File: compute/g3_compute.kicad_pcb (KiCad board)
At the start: 4 copper layers, 100 x 100 mm, 36 parts, among them J101 CONSMA001-SMD-G, U101 PA1616D, U102 LoRa-E5, U201 SX1262, U202 PE4259, Y201 DNL

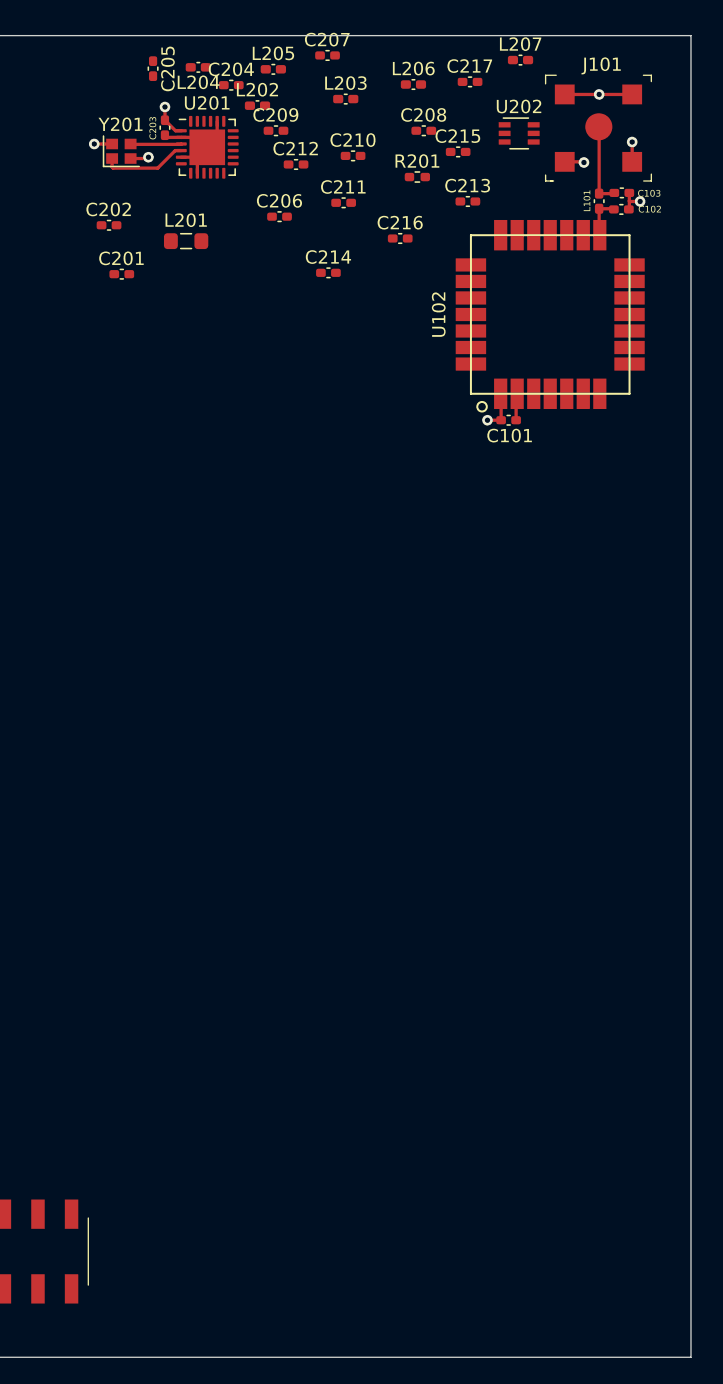
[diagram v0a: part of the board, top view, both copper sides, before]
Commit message: Finish LoRa routing
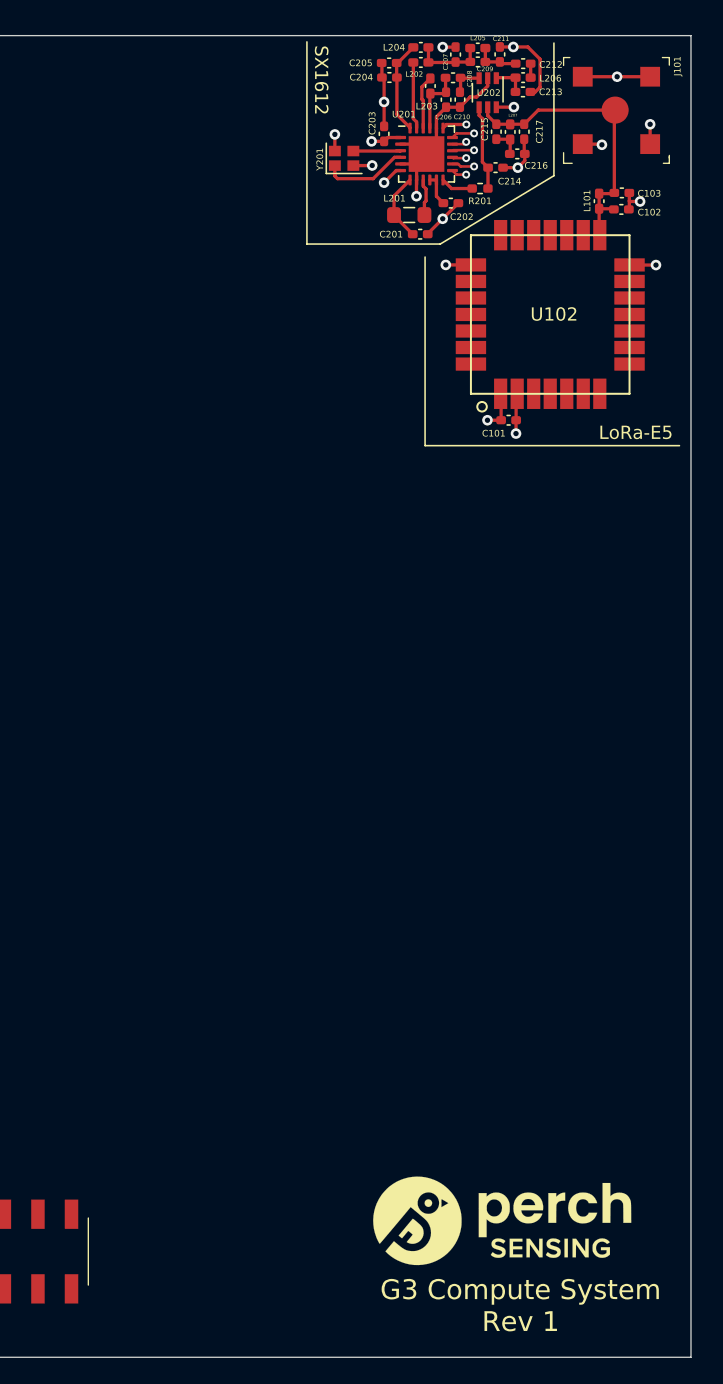
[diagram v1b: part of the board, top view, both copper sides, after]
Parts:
- added G***: LOGO, Perch:perch_logo, F.Cu at (185.8, 129.8)
- moved C202 25.9 mm to (181.8, 52.7)
- moved C201 22.8 mm to (179.5, 55.0)
- moved C212 18.8 mm to (187.3, 42.1)
- moved C205 17.9 mm to (177.2, 42.1), turned to 180 degrees
- moved L201 17.0 mm to (178.7, 53.6)
- moved L204 16.9 mm to (179.6, 40.9)
- moved Y201 16.9 mm to (173.8, 49.3)
- moved U201 16.6 mm to (180.0, 49.0)
- moved C203 16.6 mm to (176.8, 47.4), turned to 90 degrees
- moved C211 16.3 mm to (185.5, 41.4), turned to 90 degrees
- moved C209 16.1 mm to (183.9, 42.0)
- moved L205 15.6 mm to (183.9, 40.9)
- moved C206 15.4 mm to (181.5, 44.9), turned to 270 degrees
- moved C214 14.9 mm to (185.2, 50.0)
- moved L202 12.8 mm to (179.6, 42.0)
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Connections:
- C215 pad 1: Net-(C215-Pad1) -> /ANT
- U202 pad 5: Net-(C215-Pad1) -> /ANT
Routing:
- net GND: track 24.3 -> 54.5 mm, vias 6 -> 15
- net /ANT: track 9.39 -> 22.9 mm
- net Net-(C204-Pad1): track 0.00 -> 7.09 mm
- net Net-(C214-Pad1): track 0.00 -> 6.44 mm
- net Net-(C207-Pad1): track 0.00 -> 5.38 mm
- net Net-(C201-Pad1): track 0.00 -> 5.19 mm
- net Net-(L202-Pad1): track 0.00 -> 5.07 mm
- net Net-(C206-Pad1): track 0.00 -> 4.97 mm
- net Net-(L203-Pad1): track 0.00 -> 4.14 mm
- net Net-(C209-Pad2): track 0.00 -> 3.58 mm
- net Net-(L201-Pad2): track 0.00 -> 2.79 mm
- net Net-(C213-Pad1): track 0.00 -> 2.60 mm
- net Net-(C208-Pad2): track 0.00 -> 2.52 mm
- net /LoRa Module/DIO2: track 0.00 -> 2.47 mm
- net Net-(C202-Pad1): track 0.00 -> 2.47 mm
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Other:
- board text added: "G3 Compute System Rev 1"
- board text added: "LoRa-E5"
- board text added: "SX1612"

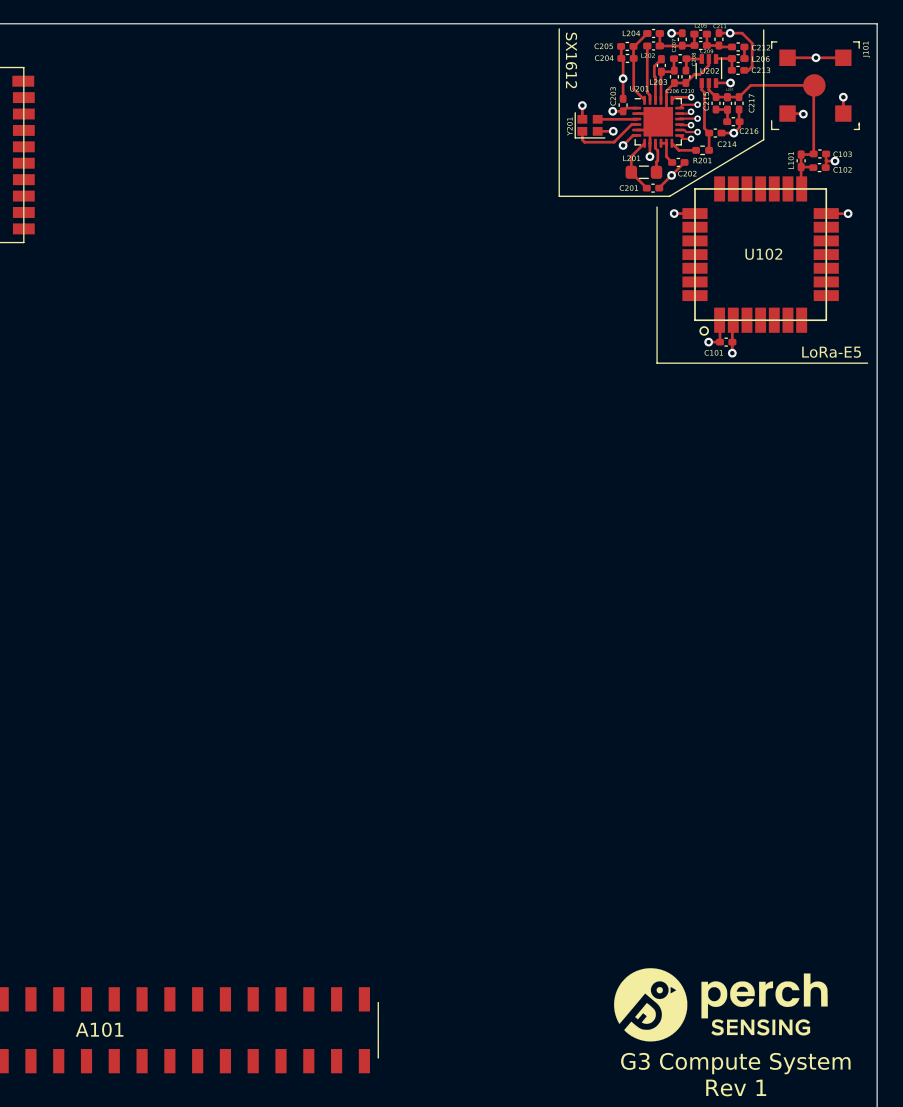
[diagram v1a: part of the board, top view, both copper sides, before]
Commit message: Fixing libraries and schematic ref nums
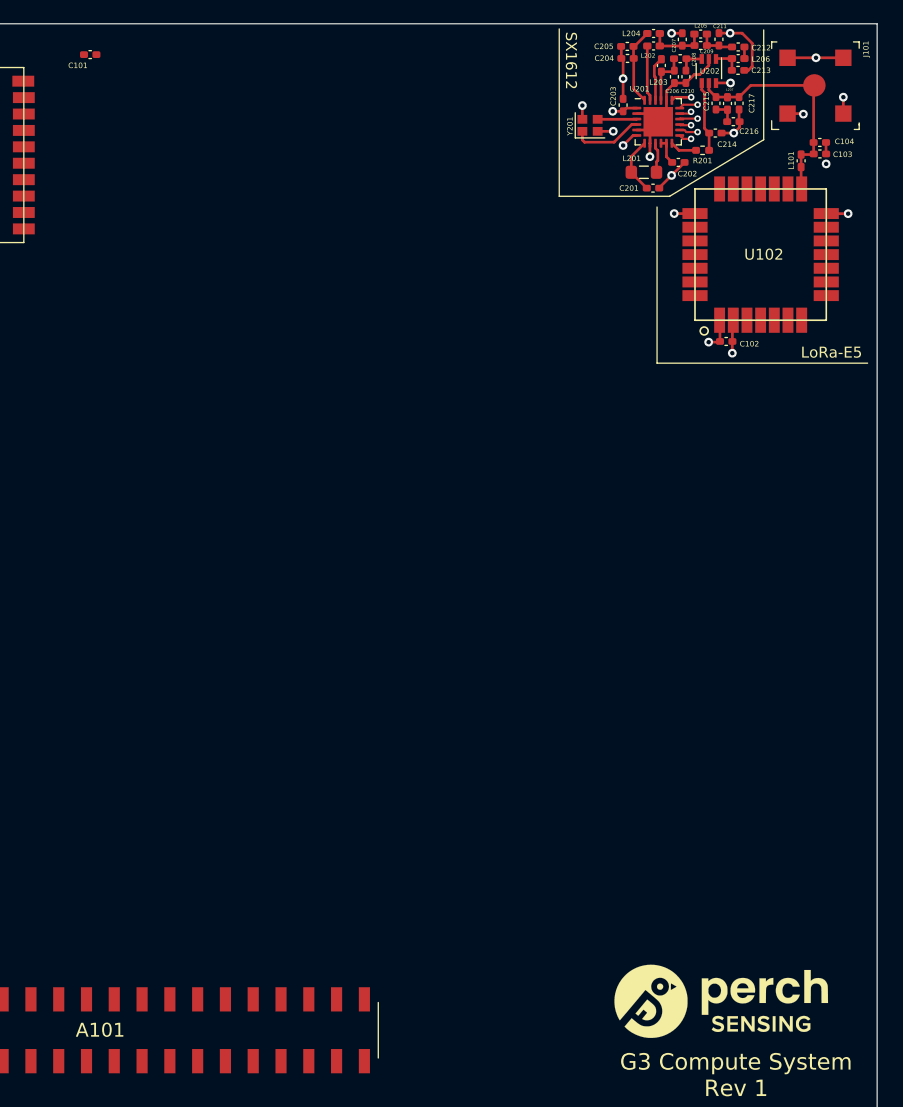
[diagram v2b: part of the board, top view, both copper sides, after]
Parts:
- added C104: DNL, Capacitor_SMD:C_0402_1005Metric_Pad0.74x0.62mm_HandSolder, F.Cu at (194.8, 50.9)
- C102: value DNL -> 4.7uF
- moved C101 63.8 mm to (128.1, 42.8)
- moved C102 18.0 mm to (186.2, 69.0)
- moved G*** 0.32 mm to (185.9, 129.4)
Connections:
- net Net-(U101-Pad1) renamed /GPS_Switch/VOUT
- net Net-(U101-Pad2) renamed /~GPS_RESET
- C102 pad 1: /ANT -> 3V3
- U101 pad 12: Net-(U101-Pad12) -> GND
- U101 pad 19: Net-(U101-Pad19) -> GND
- U101 pad 8: Net-(U101-Pad8) -> Net-(U101-Pad3)
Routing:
- net GND: track 54.5 -> 53.4 mm
- net /ANT: track 22.9 -> 21.9 mm

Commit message: rework on sch and layout
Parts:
- added C101: 1uF, Capacitor_SMD:C_0402_1005Metric_Pad0.74x0.62mm_HandSolder, F.Cu at (128.7, 79.1)
- added C105: 1uF, Capacitor_SMD:C_0402_1005Metric_Pad0.74x0.62mm_HandSolder, F.Cu at (125.4, 83.0)
- added J102: Temp_Connector_1x4, Perch:1702474_Temp_Sensor_Connector, F.Cu at (112.1, 74.9)
- added R101: 470, Resistor_SMD:R_0402_1005Metric_Pad0.72x0.64mm_HandSolder, F.Cu at (125.4, 73.1)
- added R102: 470, Resistor_SMD:R_0402_1005Metric_Pad0.72x0.64mm_HandSolder, F.Cu at (125.4, 75.1)
- added R103: TBD, Resistor_SMD:R_0402_1005Metric_Pad0.72x0.64mm_HandSolder, F.Cu at (128.7, 73.1)
- added R104: TBD, Resistor_SMD:R_0402_1005Metric_Pad0.72x0.64mm_HandSolder, F.Cu at (125.4, 77.1)
- added R105: 0, Resistor_SMD:R_0402_1005Metric_Pad0.72x0.64mm_HandSolder, F.Cu at (128.7, 75.1)
- added R106: 0, Resistor_SMD:R_0402_1005Metric_Pad0.72x0.64mm_HandSolder, F.Cu at (125.4, 79.1)
- added R107: 22, Resistor_SMD:R_0402_1005Metric_Pad0.72x0.64mm_HandSolder, F.Cu at (128.7, 77.1)
- added R108: 22, Resistor_SMD:R_0402_1005Metric_Pad0.72x0.64mm_HandSolder, F.Cu at (125.4, 81.1)
- renumbered C101 to C102
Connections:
- net /LoRa Module/SCK renamed /PI_SCLK
- net /LoRa Module/SDI renamed /PI_SDO
- net /LoRa Module/~CS renamed /~PI_CE0
- net /LoRa Module/~RESET renamed /~SX_RESET
- net Net-(U102-Pad17) renamed /~E5_RESET
- C103 pad 1: /ANT -> /E5_RFIO
- L101 pad 1: /ANT -> /E5_RFIO
- U101 pad 1: /GPS_Switch/VOUT -> /GPS_VCC
- U101 pad 10: Net-(R102-Pad1) -> /GPS_RX0
- U101 pad 3: Net-(U101-Pad3) -> GND
- U101 pad 8: Net-(U101-Pad3) -> GND
- U101 pad 9: Net-(R101-Pad1) -> /GPS_TX0
- U102 pad 10: Net-(U102-Pad10) -> /E5_TX
- U102 pad 15: /ANT -> /E5_RFIO
- U102 pad 9: Net-(U102-Pad9) -> /E5_RX
- U201 pad 16: /LoRa Module/SDO -> /PI_SDI
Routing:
- net /PI_SDI: track 0.00 -> 1.49 mm, vias 0 -> 1
- net /LoRa Module/SDO: track 1.49 -> 0.00 mm, vias 1 -> 0
